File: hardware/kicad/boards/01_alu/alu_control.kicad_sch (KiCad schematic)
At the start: 4 parts, among them U161 28C256, U162 28C256

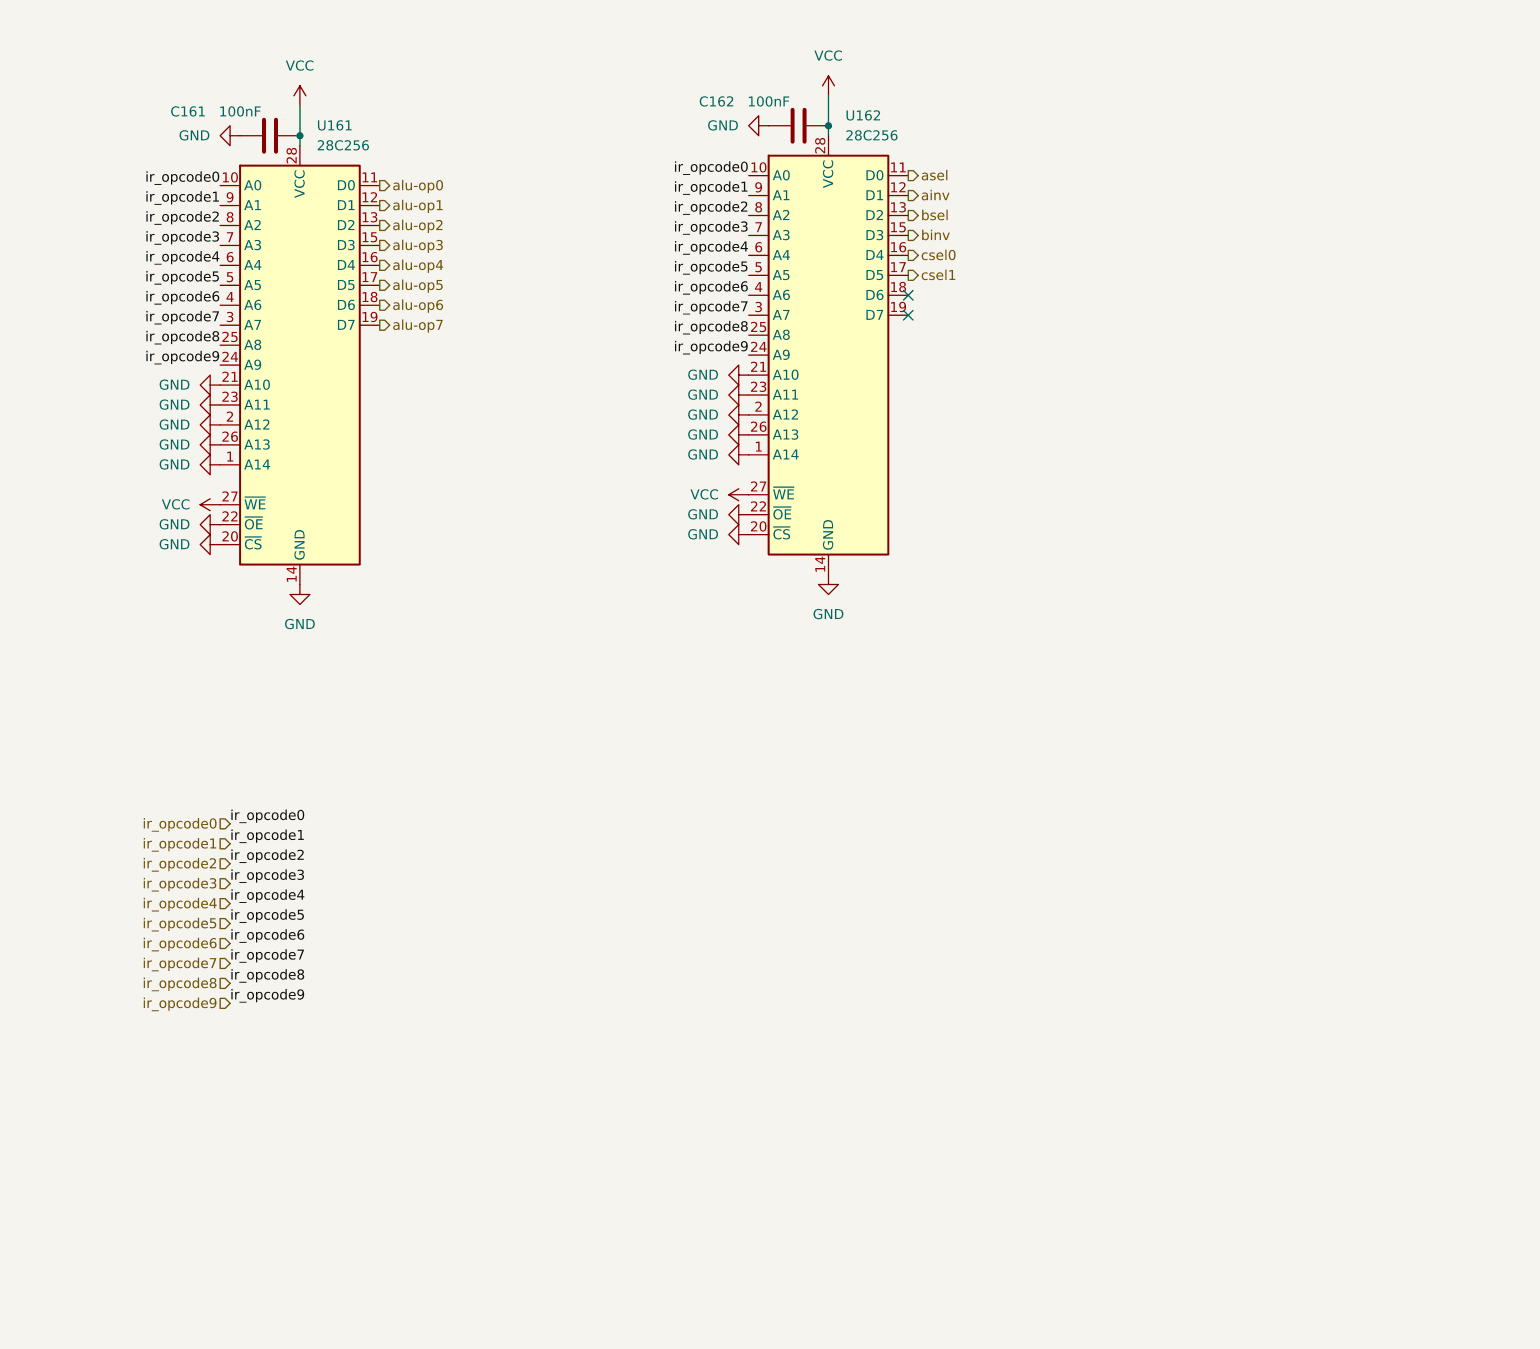
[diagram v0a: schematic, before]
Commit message: kicad: checkpoint; designed the alu display logic; clock circuit
Added registers for each display to ensure robustness and less worry about debugging screen, keeping focus on the alu board and other components
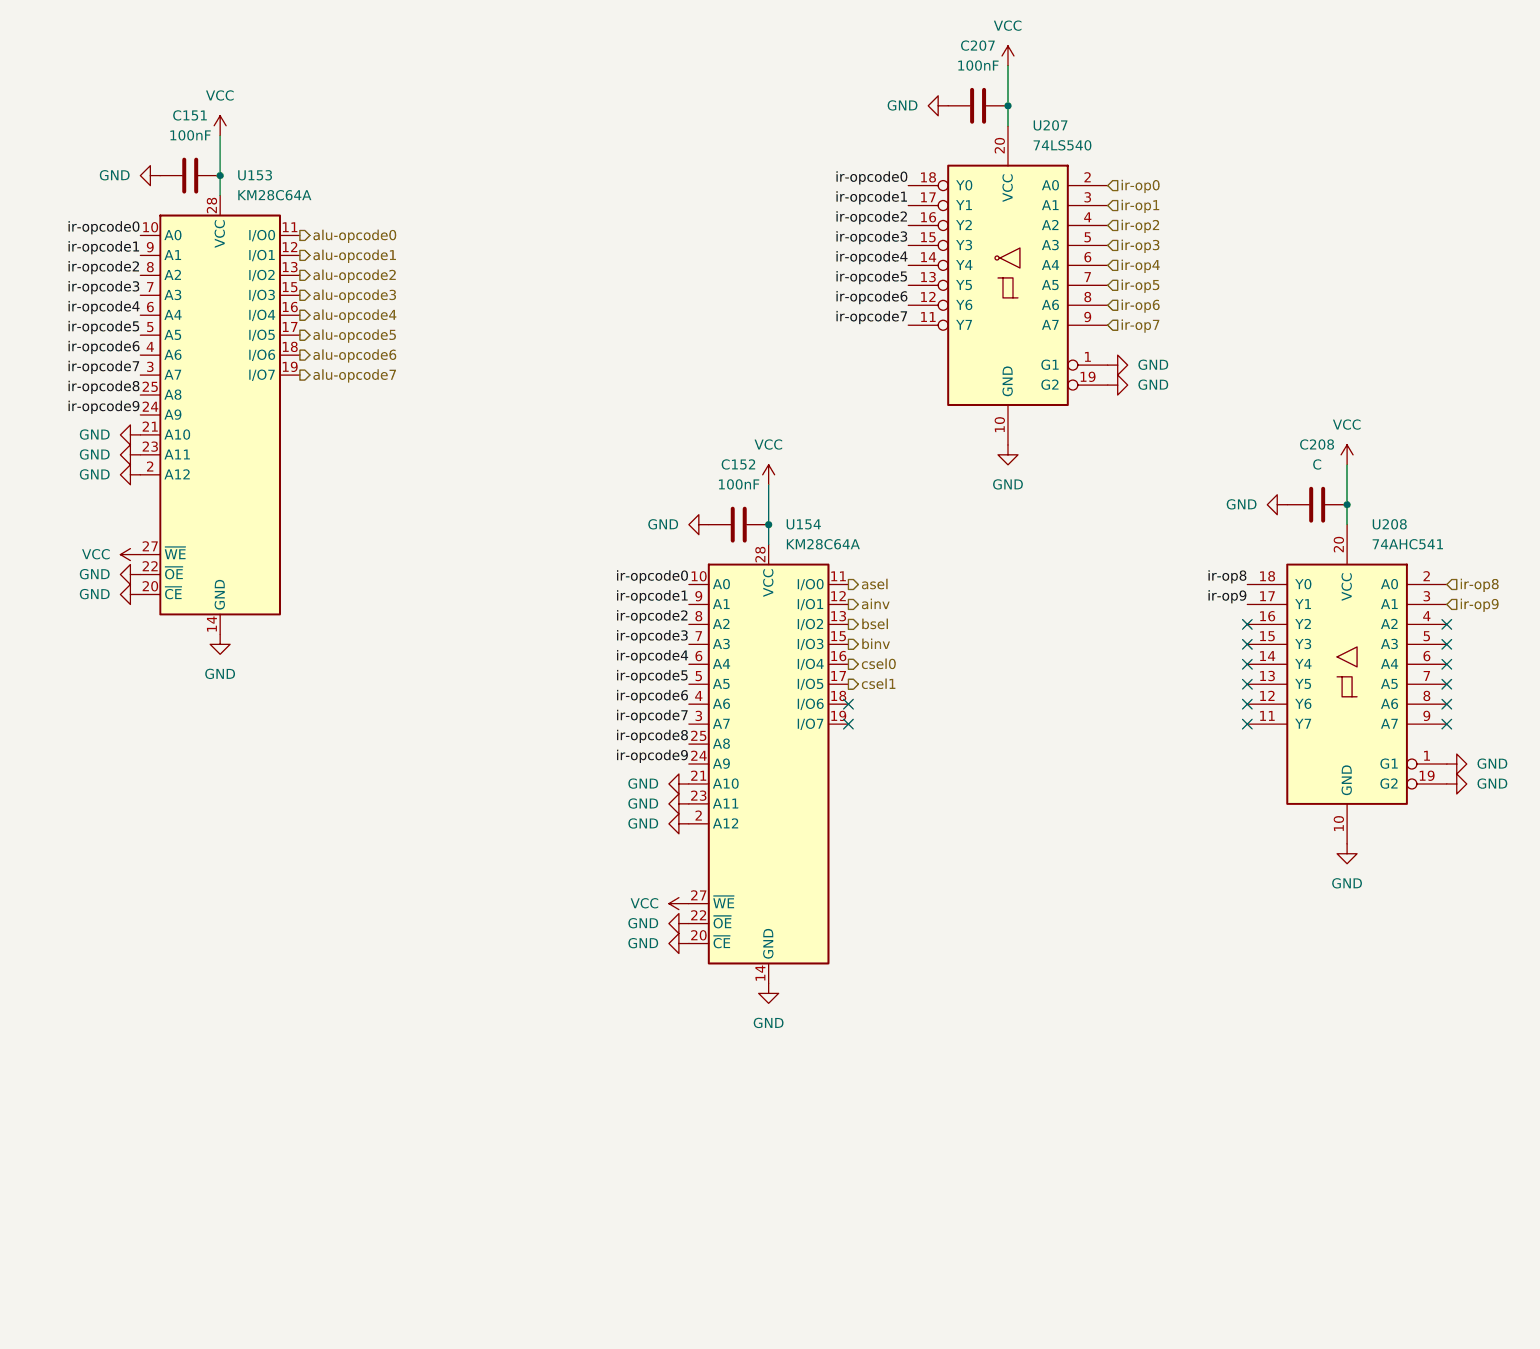
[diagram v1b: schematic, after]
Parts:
- removed C161, C162: 100nF, Capacitor_SMD:C_0805_2012Metric, symbol Device:C
- removed U161, U162: 28C256, Package_SO:SOIC-28W_7.5x17.9mm_P1.27mm, symbol Memory_EEPROM:28C256
- added C151, C152, C207: 100nF, Capacitor_SMD:C_0805_2012Metric, symbol Device:C
- added C208: C, Capacitor_SMD:C_0805_2012Metric, symbol Device:C
- added U153, U154: KM28C64A, Package_DIP:DIP-28_W15.24mm, symbol Memory_EEPROM:KM28C64A
- added U207: 74LS540, Package_SO:SOIC-20W_7.5x12.8mm_P1.27mm, symbol 74xx:74LS540
- added U208: 74AHC541, Package_SO:SOIC-20W_7.5x12.8mm_P1.27mm, symbol 74xx:74AHC541
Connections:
- net GND: now also C151.1, C152.1, C207.1, C208.1, U153.14 (GND), U153.2 (A12), U153.20 (~{CE}), U153.21 (A10), U153.22 (~{OE}), U153.23 (A11), U154.14 (GND), U154.2 (A12), U154.20 (~{CE}), U154.21 (A10), U154.22 (~{OE}), U154.23 (A11), U207.1 (G1), U207.10 (GND), U207.19 (G2), U208.1 (G1), U208.10 (GND), U208.19 (G2)
- net VCC: now also C151.2, C152.2, C207.2, C208.2, U153.27 (~{WE}), U153.28 (VCC), U154.27 (~{WE}), U154.28 (VCC), U207.20 (VCC), U208.20 (VCC)
- net ainv: now also U154.12 (I/O1)
- net asel: now also U154.11 (I/O0)
- net binv: now also U154.15 (I/O3)
- net bsel: now also U154.13 (I/O2)
- net csel0: now also U154.16 (I/O4)
- net csel1: now also U154.17 (I/O5)
- new net alu-opcode0: U153.11 (I/O0)
- new net alu-opcode1: U153.12 (I/O1)
- new net alu-opcode2: U153.13 (I/O2)
- new net alu-opcode3: U153.15 (I/O3)
- new net alu-opcode4: U153.16 (I/O4)
- new net alu-opcode5: U153.17 (I/O5)
- new net alu-opcode6: U153.18 (I/O6)
- new net alu-opcode7: U153.19 (I/O7)
- new net ir-op0: U207.2 (A0)
- new net ir-op1: U207.3 (A1)
- new net ir-op2: U207.4 (A2)
- new net ir-op3: U207.5 (A3)
- new net ir-op4: U207.6 (A4)
- new net ir-op5: U207.7 (A5)
- new net ir-op6: U207.8 (A6)
- new net ir-op7: U207.9 (A7)
- new net ir-op8: U208.18 (Y0), U208.2 (A0)
- new net ir-op9: U208.17 (Y1), U208.3 (A1)
- new net ir-opcode0: U153.10 (A0), U154.10 (A0), U207.18 (Y0)
- new net ir-opcode1: U153.9 (A1), U154.9 (A1), U207.17 (Y1)
- new net ir-opcode2: U153.8 (A2), U154.8 (A2), U207.16 (Y2)
- new net ir-opcode3: U153.7 (A3), U154.7 (A3), U207.15 (Y3)
- new net ir-opcode4: U153.6 (A4), U154.6 (A4), U207.14 (Y4)
- new net ir-opcode5: U153.5 (A5), U154.5 (A5), U207.13 (Y5)
- new net ir-opcode6: U153.4 (A6), U154.4 (A6), U207.12 (Y6)
- new net ir-opcode7: U153.3 (A7), U154.3 (A7), U207.11 (Y7)
- new net ir-opcode8: U153.25 (A8), U154.25 (A8)
- new net ir-opcode9: U153.24 (A9), U154.24 (A9)
- no-connect marks 2 -> 14

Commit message: alu: completed all core schematics; DRC and ERC pending 🎉
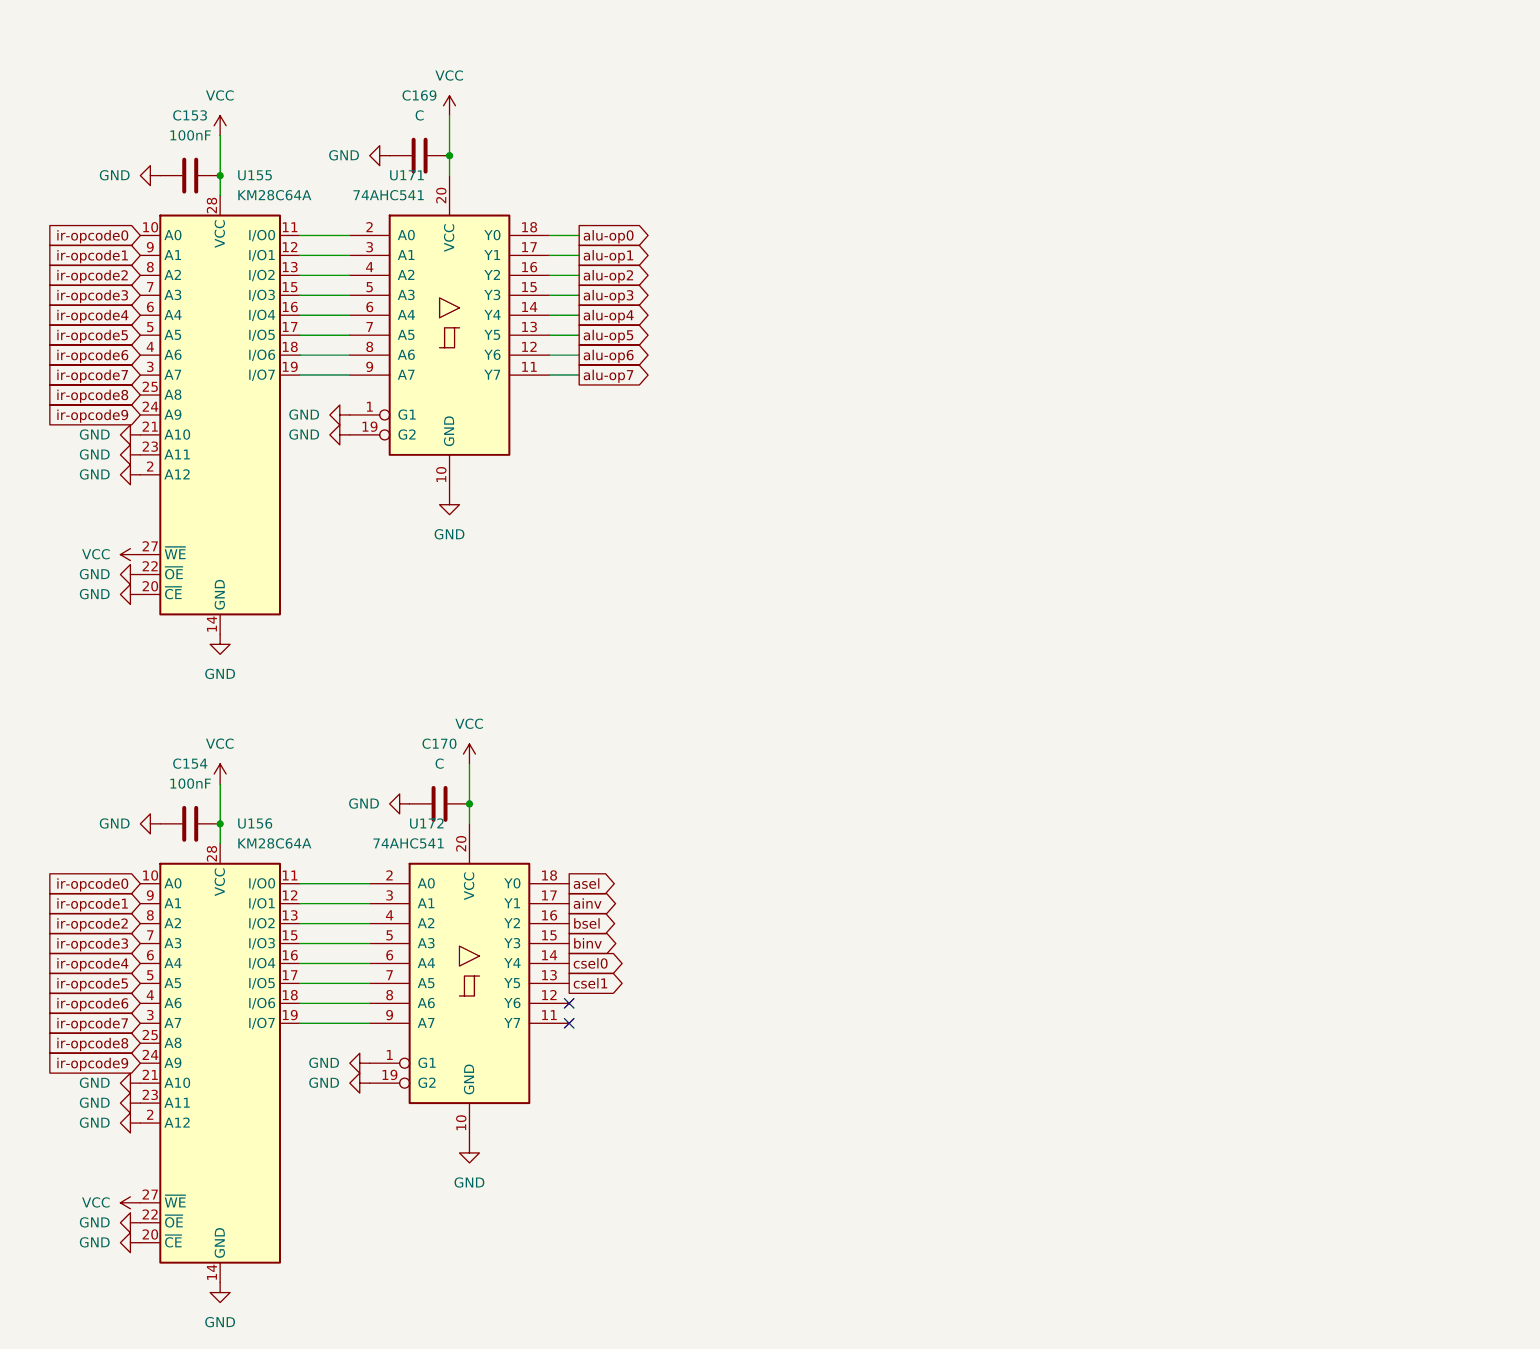
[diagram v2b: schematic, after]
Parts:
- removed C207: 100nF, Capacitor_SMD:C_0805_2012Metric, symbol Device:C
- removed C208: C, Capacitor_SMD:C_0805_2012Metric, symbol Device:C
- removed U207: 74LS540, Package_SO:SOIC-20W_7.5x12.8mm_P1.27mm, symbol 74xx:74LS540
- removed U208: 74AHC541, Package_SO:SOIC-20W_7.5x12.8mm_P1.27mm, symbol 74xx:74AHC541
- added C169, C170: C, Capacitor_SMD:C_0805_2012Metric, symbol Device:C
- added U171, U172: 74AHC541, Package_SO:SOIC-20W_7.5x12.8mm_P1.27mm, symbol 74xx:74AHC541
- renumbered C151 to C153, C152 to C154, U153 to U155, U154 to U156
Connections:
- net GND: now also C169.1, C170.1, U171.1 (G1), U171.10 (GND), U171.19 (G2), U172.1 (G1), U172.10 (GND), U172.19 (G2)
- net VCC: now also C169.2, C170.2, U171.20 (VCC), U172.20 (VCC)
- net ainv: now also U172.17 (Y1); no longer U156.12 (I/O1)
- net asel: now also U172.18 (Y0); no longer U156.11 (I/O0)
- net binv: now also U172.15 (Y3); no longer U156.15 (I/O3)
- net bsel: now also U172.16 (Y2); no longer U156.13 (I/O2)
- net csel0: now also U172.14 (Y4); no longer U156.16 (I/O4)
- net csel1: now also U172.13 (Y5); no longer U156.17 (I/O5)
- net at U156.18 (I/O6): now also U172.8 (A6)
- net at U156.19 (I/O7): now also U172.9 (A7)
- net alu-opcode0: no longer names the net of U155.11 (I/O0)
- net alu-opcode0: now also U171.2 (A0)
- net alu-opcode1: no longer names the net of U155.12 (I/O1)
- net alu-opcode1: now also U171.3 (A1)
- net alu-opcode2: no longer names the net of U155.13 (I/O2)
- net alu-opcode2: now also U171.4 (A2)
- net alu-opcode3: no longer names the net of U155.15 (I/O3)
- net alu-opcode3: now also U171.5 (A3)
- net alu-opcode4: no longer names the net of U155.16 (I/O4)
- net alu-opcode4: now also U171.6 (A4)
- net alu-opcode5: no longer names the net of U155.17 (I/O5)
- net alu-opcode5: now also U171.7 (A5)
- net alu-opcode6: no longer names the net of U155.18 (I/O6)
- net alu-opcode6: now also U171.8 (A6)
- net alu-opcode7: no longer names the net of U155.19 (I/O7)
- net alu-opcode7: now also U171.9 (A7)
- new net: U156.11 (I/O0), U172.2 (A0)
- new net: U156.12 (I/O1), U172.3 (A1)
- new net: U156.13 (I/O2), U172.4 (A2)
- new net: U156.15 (I/O3), U172.5 (A3)
- new net: U156.16 (I/O4), U172.6 (A4)
- new net: U156.17 (I/O5), U172.7 (A5)
- new net alu-op0: U171.18 (Y0)
- new net alu-op1: U171.17 (Y1)
- new net alu-op2: U171.16 (Y2)
- new net alu-op3: U171.15 (Y3)
- new net alu-op4: U171.14 (Y4)
- new net alu-op5: U171.13 (Y5)
- new net alu-op6: U171.12 (Y6)
- new net alu-op7: U171.11 (Y7)
- no-connect marks 14 -> 2
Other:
- moved on the sheet: C154, U156
